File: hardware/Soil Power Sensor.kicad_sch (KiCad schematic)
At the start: 0 parts

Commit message: Replaced resistor symbols
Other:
- company: (none) -> jlab
- title: (none) -> Soil Power Sensor
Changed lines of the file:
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@@
 (kicad_sch (version 20230121) (generator eeschema)
   (paper "A4")
+  (title_block
+    (title "Soil Power Sensor")
+    (date "2023-09-15")
+    (rev "2.1.0")
+    (company "jlab")
+  )
   (sheet (at 177.8 25.4) (size 12.7 3.81) (fields_autoplaced)
     (stroke (width 0) (type solid))

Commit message: Updated hierarchical sheets
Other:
- sheet Soil Power Sensor_1 renamed Analog
- sheet Soil Power Sensor_2 renamed Power
- sheet Soil Power Sensor_3 renamed STM32
- sheet Soil Power Sensor_4 renamed ESP32
- sheet Analog ports: added ADC_DRDY, SCL, SDA; removed none
- sheet ESP32 ports: added ESP32_EN, SCL, SDA; removed none
- sheet Power ports: added POWERDOWN; removed none
- sheet STM32 ports: added ADC_DRDY, ESP32_EN, POWERDOWN, SCL, SDA; removed none
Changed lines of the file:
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@@
     (company "jlab")
   )
-  (sheet (at 177.8 25.4) (size 12.7 3.81) (fields_autoplaced)
+  (junction (at 152.4 74.93) (diameter 0) (color 0 0 0 0)
+  )
+  (junction (at 149.86 77.47) (diameter 0) (color 0 0 0 0)
+  )
+  (wire (pts (xy 137.16 81.28) (xy 162.56 81.28))
+    (stroke (width 0) (type default))
+  )
+  (wire (pts (xy 149.86 77.47) (xy 162.56 77.47))
+    (stroke (width 0) (type default))
+  )
+  (wire (pts (xy 162.56 97.79) (xy 149.86 97.79))
+    (stroke (width 0) (type default))
+  )
+  (wire (pts (xy 152.4 74.93) (xy 162.56 74.93))
+    (stroke (width 0) (type default))
+  )
+  (wire (pts (xy 137.16 74.93) (xy 152.4 74.93))
+    (stroke (width 0) (type default))
+  )
+  (wire (pts (xy 152.4 95.25) (xy 152.4 74.93))
+    (stroke (width 0) (type default))
+  )
+  (wire (pts (xy 137.16 101.6) (xy 162.56 101.6))
+    (stroke (width 0) (type default))
+  )
+  (wire (pts (xy 137.16 77.47) (xy 149.86 77.47))
+    (stroke (width 0) (type default))
+  )
+  (wire (pts (xy 149.86 97.79) (xy 149.86 77.47))
+    (stroke (width 0) (type default))
+  )
+  (wire (pts (xy 162.56 95.25) (xy 152.4 95.25))
+    (stroke (width 0) (type default))
+  )
+  (wire (pts (xy 137.16 115.57) (xy 162.56 115.57))
+    (stroke (width 0) (type default))
+  )
+  (sheet (at 162.56 92.71) (size 16.51 11.43) (fields_autoplaced)
     (stroke (width 0) (type solid))
     (fill (color 0 0 0 0.0000))
-    (property "Sheetname" "Soil Power Sensor_4" (at 177.8 24.6884 0)
+    (property "Sheetname" "ESP32" (at 162.56 91.9984 0)
       (effects (font (size 1.27 1.27)) (justify left bottom))
     )
-    (property "Sheetfile" "Soil_Power_Sensor_4.kicad_sch" (at 177.8 29.7946 0)
+    (property "Sheetfile" "Soil_Power_Sensor_4.kicad_sch" (at 162.56 104.7246 0)
       (effects (font (size 1.27 1.27)) (justify left top))
+    )
+    (pin "ESP32_EN" input (at 162.56 101.6 180)
+      (effects (font (size 1.27 1.27)) (justify left))
+    )
+    (pin "SCL" bidirectional (at 162.56 97.79 180)
+      (effects (font (size 1.27 1.27)) (justify left))
+    )
+    (pin "SDA" bidirectional (at 162.56 95.25 180)
+      (effects (font (size 1.27 1.27)) (justify left))
     )
     (instances
@@
     )
   )
-  (sheet (at 127 25.4) (size 12.7 3.81) (fields_autoplaced)
+  (sheet (at 119.38 72.39) (size 17.78 45.72) (fields_autoplaced)
     (stroke (width 0) (type solid))
     (fill (color 0 0 0 0.0000))
-    (property "Sheetname" "Soil Power Sensor_3" (at 127 24.6884 0)
+    (property "Sheetname" "STM32" (at 119.38 71.6784 0)
       (effects (font (size 1.27 1.27)) (justify left bottom))
     )
-    (property "Sheetfile" "Soil_Power_Sensor_3.kicad_sch" (at 127 29.7946 0)
+    (property "Sheetfile" "Soil_Power_Sensor_3.kicad_sch" (at 119.38 118.6946 0)
       (effects (font (size 1.27 1.27)) (justify left top))
+    )
+    (pin "ESP32_EN" output (at 137.16 101.6 0)
+      (effects (font (size 1.27 1.27)) (justify right))
+    )
+    (pin "ADC_DRDY" input (at 137.16 81.28 0)
+      (effects (font (size 1.27 1.27)) (justify right))
+    )
+    (pin "SDA" bidirectional (at 137.16 74.93 0)
+      (effects (font (size 1.27 1.27)) (justify right))
+    )
+    (pin "SCL" bidirectional (at 137.16 77.47 0)
+      (effects (font (size 1.27 1.27)) (justify right))
+    )
+    (pin "POWERDOWN" output (at 137.16 115.57 0)
+      (effects (font (size 1.27 1.27)) (justify right))
     )
     (instances
@@
     )
   )
-  (sheet (at 76.2 25.4) (size 12.7 3.81) (fields_autoplaced)
+  (sheet (at 162.56 113.03) (size 16.51 5.08) (fields_autoplaced)
     (stroke (width 0) (type solid))
     (fill (color 0 0 0 0.0000))
-    (property "Sheetname" "Soil Power Sensor_2" (at 76.2 24.6884 0)
+    (property "Sheetname" "Power" (at 162.56 112.3184 0)
       (effects (font (size 1.27 1.27)) (justify left bottom))
     )
-    (property "Sheetfile" "Soil_Power_Sensor_2.kicad_sch" (at 76.2 29.7946 0)
+    (property "Sheetfile" "Soil_Power_Sensor_2.kicad_sch" (at 162.56 118.6946 0)
       (effects (font (size 1.27 1.27)) (justify left top))
+    )
+    (pin "POWERDOWN" input (at 162.56 115.57 180)
+      (effects (font (size 1.27 1.27)) (justify left))
     )
     (instances
@@
     )
   )
-  (sheet (at 25.4 25.4) (size 12.7 3.81) (fields_autoplaced)
+  (sheet (at 162.56 72.39) (size 16.51 11.43) (fields_autoplaced)
     (stroke (width 0) (type solid))
     (fill (color 0 0 0 0.0000))
-    (property "Sheetname" "Soil Power Sensor_1" (at 25.4 24.6884 0)
+    (property "Sheetname" "Analog" (at 162.56 71.6784 0)
       (effects (font (size 1.27 1.27)) (justify left bottom))
     )
-    (property "Sheetfile" "Soil_Power_Sensor_1.kicad_sch" (at 25.4 29.7946 0)
+    (property "Sheetfile" "Soil_Power_Sensor_1.kicad_sch" (at 162.56 84.4046 0)
       (effects (font (size 1.27 1.27)) (justify left top))
     )
+    (pin "ADC_DRDY" output (at 162.56 81.28 180)
+      (effects (font (size 1.27 1.27)) (justify left))
+    )
+    (pin "SCL" bidirectional (at 162.56 77.47 180)
+      (effects (font (size 1.27 1.27)) (justify left))
+    )
+    (pin "SDA" bidirectional (at 162.56 74.93 180)
+      (effects (font (size 1.27 1.27)) (justify left))
+    )
     (instances

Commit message: Updated PCB
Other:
- sheet Analog ports: added POWERDOWN; removed none
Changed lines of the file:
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@@
     (company "jlab")
+  )
+  (junction (at 149.86 81.28) (diameter 0) (color 0 0 0 0)
+  )
+  (junction (at 154.94 118.745) (diameter 0) (color 0 0 0 0)
   )
   (junction (at 152.4 74.93) (diameter 0) (color 0 0 0 0)
@@
   (junction (at 149.86 77.47) (diameter 0) (color 0 0 0 0)
   )
-  (wire (pts (xy 137.16 81.28) (xy 162.56 81.28))
+  (wire (pts (xy 137.16 81.28) (xy 149.86 81.28))
     (stroke (width 0) (type default))
   )
@@
     (stroke (width 0) (type default))
   )
-  (wire (pts (xy 162.56 97.79) (xy 149.86 97.79))
+  (wire (pts (xy 162.56 100.965) (xy 149.86 100.965))
     (stroke (width 0) (type default))
   )
@@
     (stroke (width 0) (type default))
   )
-  (wire (pts (xy 152.4 95.25) (xy 152.4 74.93))
+  (wire (pts (xy 162.56 85.09) (xy 154.94 85.09))
     (stroke (width 0) (type default))
   )
-  (wire (pts (xy 137.16 101.6) (xy 162.56 101.6))
+  (wire (pts (xy 154.94 85.09) (xy 154.94 118.745))
+    (stroke (width 0) (type default))
+  )
+  (wire (pts (xy 149.86 77.47) (xy 149.86 81.28))
+    (stroke (width 0) (type default))
+  )
+  (wire (pts (xy 149.86 81.28) (xy 162.56 81.28))
+    (stroke (width 0) (type default))
+  )
+  (wire (pts (xy 137.16 104.775) (xy 162.56 104.775))
     (stroke (width 0) (type default))
   )
@@
     (stroke (width 0) (type default))
   )
-  (wire (pts (xy 149.86 97.79) (xy 149.86 77.47))
+  (wire (pts (xy 154.94 118.745) (xy 162.56 118.745))
     (stroke (width 0) (type default))
   )
-  (wire (pts (xy 162.56 95.25) (xy 152.4 95.25))
+  (wire (pts (xy 149.86 100.965) (xy 149.86 81.28))
     (stroke (width 0) (type default))
   )
-  (wire (pts (xy 137.16 115.57) (xy 162.56 115.57))
+  (wire (pts (xy 162.56 98.425) (xy 152.4 98.425))
     (stroke (width 0) (type default))
   )
-  (sheet (at 162.56 92.71) (size 16.51 11.43) (fields_autoplaced)
+  (wire (pts (xy 152.4 74.93) (xy 152.4 98.425))
+    (stroke (width 0) (type default))
+  )
+  (wire (pts (xy 137.16 118.745) (xy 154.94 118.745))
+    (stroke (width 0) (type default))
+  )
+  (sheet (at 162.56 95.885) (size 16.51 11.43) (fields_autoplaced)
     (stroke (width 0) (type solid))
     (fill (color 0 0 0 0.0000))
-    (property "Sheetname" "ESP32" (at 162.56 91.9984 0)
+    (property "Sheetname" "ESP32" (at 162.56 95.1734 0)
       (effects (font (size 1.27 1.27)) (justify left bottom))
     )
-    (property "Sheetfile" "Soil_Power_Sensor_4.kicad_sch" (at 162.56 104.7246 0)
+    (property "Sheetfile" "Soil_Power_Sensor_4.kicad_sch" (at 162.56 107.8996 0)
       (effects (font (size 1.27 1.27)) (justify left top))
     )
-    (pin "ESP32_EN" input (at 162.56 101.6 180)
+    (pin "ESP32_EN" input (at 162.56 104.775 180)
       (effects (font (size 1.27 1.27)) (justify left))
     )
-    (pin "SCL" bidirectional (at 162.56 97.79 180)
+    (pin "SCL" bidirectional (at 162.56 100.965 180)
       (effects (font (size 1.27 1.27)) (justify left))
     )
-    (pin "SDA" bidirectional (at 162.56 95.25 180)
+    (pin "SDA" bidirectional (at 162.56 98.425 180)
       (effects (font (size 1.27 1.27)) (justify left))
     )
@@
     )
   )
-  (sheet (at 119.38 72.39) (size 17.78 45.72) (fields_autoplaced)
+  (sheet (at 119.38 72.39) (size 17.78 48.895) (fields_autoplaced)
     (stroke (width 0) (type solid))
     (fill (color 0 0 0 0.0000))
@@
       (effects (font (size 1.27 1.27)) (justify left bottom))
     )
-    (property "Sheetfile" "Soil_Power_Sensor_3.kicad_sch" (at 119.38 118.6946 0)
+    (property "Sheetfile" "Soil_Power_Sensor_3.kicad_sch" (at 119.38 121.8696 0)
       (effects (font (size 1.27 1.27)) (justify left top))
     )
-    (pin "ESP32_EN" output (at 137.16 101.6 0)
+    (pin "ESP32_EN" output (at 137.16 104.775 0)
       (effects (font (size 1.27 1.27)) (justify right))
     )
@@
       (effects (font (size 1.27 1.27)) (justify right))
     )
-    (pin "POWERDOWN" output (at 137.16 115.57 0)
+    (pin "POWERDOWN" output (at 137.16 118.745 0)
       (effects (font (size 1.27 1.27)) (justify right))
     )
@@
     )
   )
-  (sheet (at 162.56 113.03) (size 16.51 5.08) (fields_autoplaced)
+  (sheet (at 162.56 116.205) (size 16.51 5.08) (fields_autoplaced)
     (stroke (width 0) (type solid))
     (fill (color 0 0 0 0.0000))
-    (property "Sheetname" "Power" (at 162.56 112.3184 0)
+    (property "Sheetname" "Power" (at 162.56 115.4934 0)
       (effects (font (size 1.27 1.27)) (justify left bottom))
     )
-    (property "Sheetfile" "Soil_Power_Sensor_2.kicad_sch" (at 162.56 118.6946 0)
+    (property "Sheetfile" "Soil_Power_Sensor_2.kicad_sch" (at 162.56 121.8696 0)
       (effects (font (size 1.27 1.27)) (justify left top))
     )
-    (pin "POWERDOWN" input (at 162.56 115.57 180)
+    (pin "POWERDOWN" input (at 162.56 118.745 180)
       (effects (font (size 1.27 1.27)) (justify left))
     )
@@
     )
   )
-  (sheet (at 162.56 72.39) (size 16.51 11.43) (fields_autoplaced)
+  (sheet (at 162.56 72.39) (size 16.51 15.24) (fields_autoplaced)
     (stroke (width 0) (type solid))
     (fill (color 0 0 0 0.0000))
@@
       (effects (font (size 1.27 1.27)) (justify left bottom))
     )
-    (property "Sheetfile" "Soil_Power_Sensor_1.kicad_sch" (at 162.56 84.4046 0)
+    (property "Sheetfile" "Soil_Power_Sensor_1.kicad_sch" (at 162.56 88.2146 0)
       (effects (font (size 1.27 1.27)) (justify left top))
     )
@@
       (effects (font (size 1.27 1.27)) (justify left))
     )
+    (pin "POWERDOWN" input (at 162.56 85.09 180)
+      (effects (font (size 1.27 1.27)) (justify left))
+    )

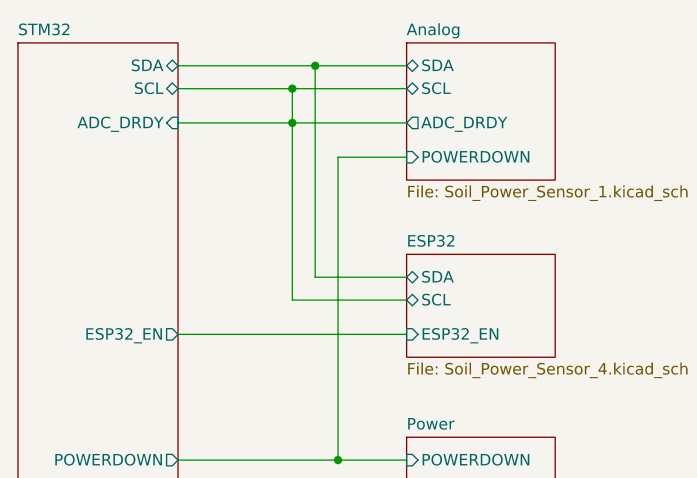
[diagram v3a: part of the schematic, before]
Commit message: Connected all nets
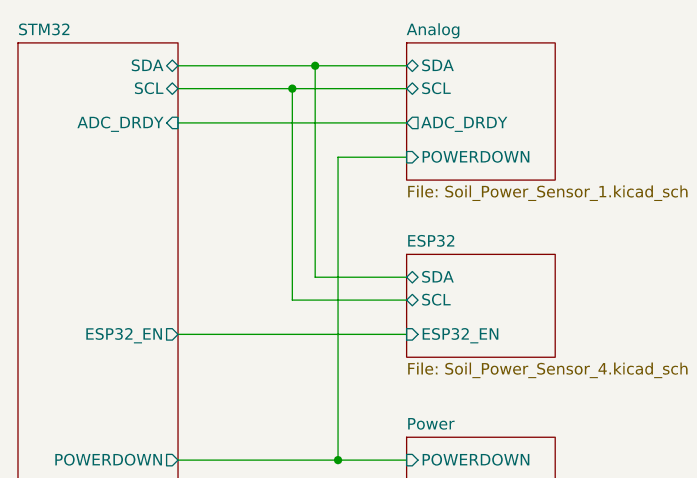
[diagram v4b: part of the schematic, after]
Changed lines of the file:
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@@
     (company "jlab")
-  )
-  (junction (at 149.86 81.28) (diameter 0) (color 0 0 0 0)
   )
   (junction (at 154.94 118.745) (diameter 0) (color 0 0 0 0)
@@
   (junction (at 149.86 77.47) (diameter 0) (color 0 0 0 0)
   )
-  (wire (pts (xy 137.16 81.28) (xy 149.86 81.28))
+  (wire (pts (xy 137.16 81.28) (xy 162.56 81.28))
     (stroke (width 0) (type default))
   )
@@
     (stroke (width 0) (type default))
   )
-  (wire (pts (xy 149.86 77.47) (xy 149.86 81.28))
-    (stroke (width 0) (type default))
-  )
-  (wire (pts (xy 149.86 81.28) (xy 162.56 81.28))
-    (stroke (width 0) (type default))
-  )
   (wire (pts (xy 137.16 104.775) (xy 162.56 104.775))
     (stroke (width 0) (type default))
@@
     (stroke (width 0) (type default))
   )
-  (wire (pts (xy 149.86 100.965) (xy 149.86 81.28))
+  (wire (pts (xy 149.86 77.47) (xy 149.86 100.965))
     (stroke (width 0) (type default))
   )
